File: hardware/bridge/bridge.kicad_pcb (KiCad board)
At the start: 2 copper layers, 45 x 80 mm, 72 parts, among them J1 XT30U-M, J10 PA5 breakout, J2 Seg A, J3 Seg B, J4 Seg C, J5 Seg D, J6 Head, J7 OLED, J8 Power button, J9 Ext 5V, Q1 NCE40P70K, Q2 2N7002, Q3 2N7002, Q4 MMBT3906, Q5 2N7002, U1 LMR51606XDBVR, U2 WeAct STM32G474 QFN48, U3 LSM6DSV16X breakout

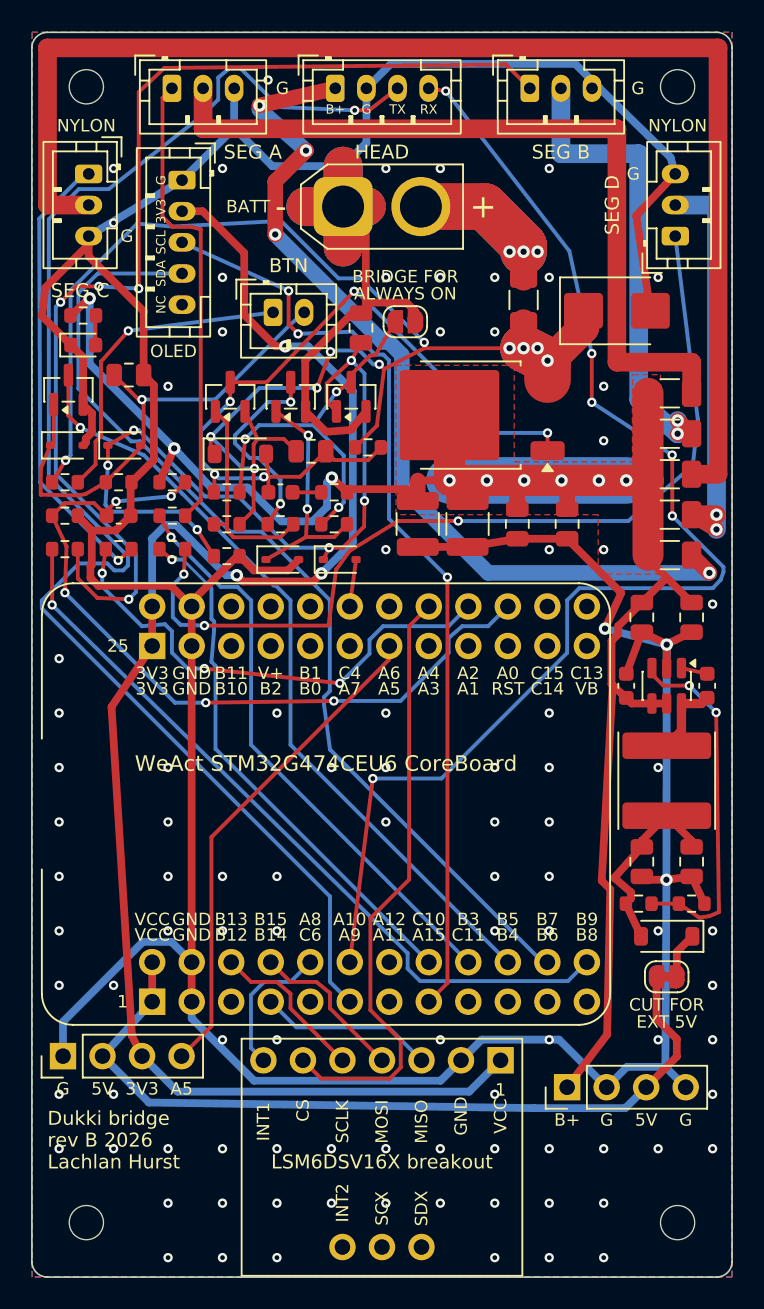
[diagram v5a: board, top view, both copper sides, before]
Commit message: Bridge PCB: second pre-order review fixes
- R14 220k to 100k (C25803, already on the board): a 70 ms tap latches
  at an 18 V pack with worst-case parts (220k needed about 150 ms).
- Buck feedback re-routed: from U1's FB pin straight to the bottom layer
  and down the west side to the divider, 17 mm, at least 1.9 mm from
  switch-node copper (it ran between the CB and SW pins and 0.22 mm
  beside L1's switch pad).
- Local copper: F3's segment B vias moved off its output pad; D2's
  ground pad solid with two stitching vias; 0.75 mm clearance round the
  XT30's + pad and a shorter ground bar beside it; JP2's ground pad on
  thermal spokes; a second via at two of VHEAD's layer changes.
- Silkscreen: J2's G above its own pin 3, clear of HEAD's B+; label
  strokes 0.15 mm; the IMU's VCC label clear of the pin-1 mark.
- Docs: the WeAct row rule in hardware/kicad/README.md, the head block
  diagram's UART direction, the carrier's exceptions in hardware.md 5.8,
  and corrected hold-up, tap and part-count figures in bridge-pcb.md.
- DRC clean with schematic parity; JLC package (30 BOM lines), PDFs and
  render regenerated.
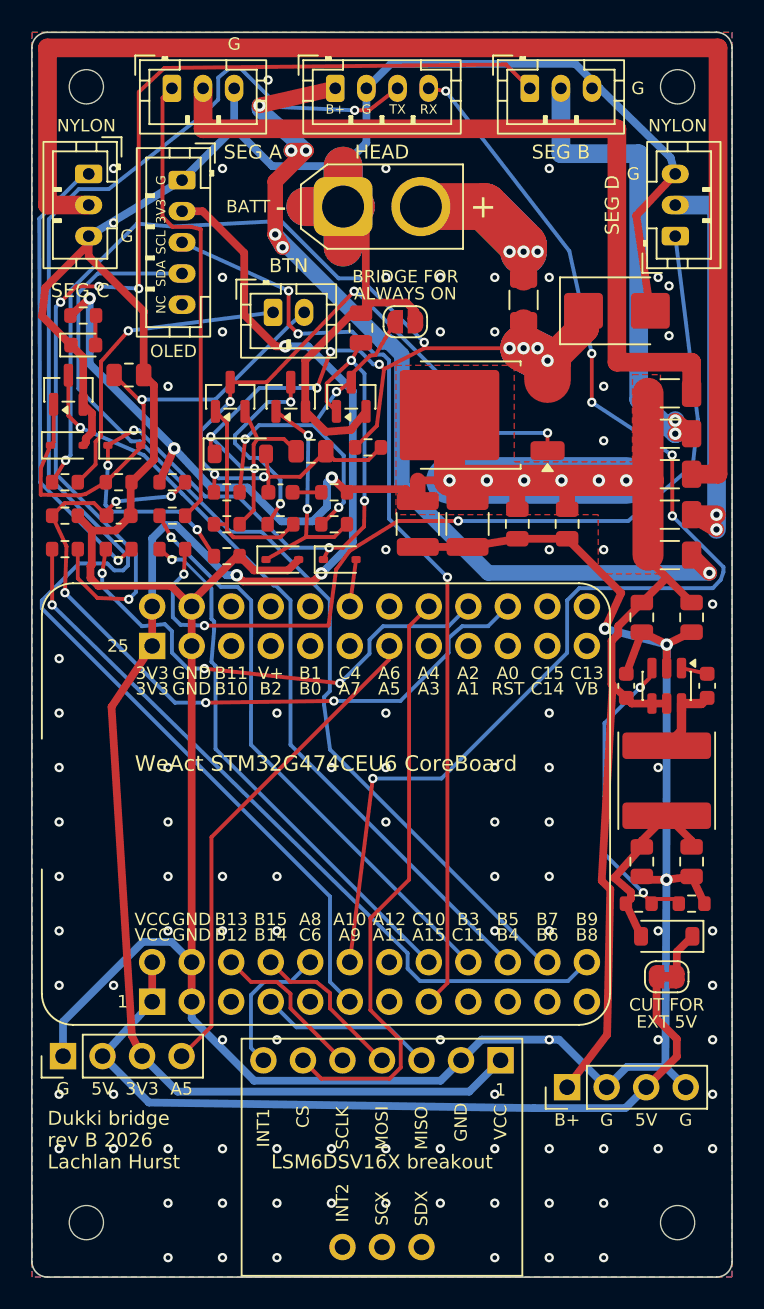
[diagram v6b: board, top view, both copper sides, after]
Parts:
- R14: value 220k -> 100k
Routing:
- net /BUCK_FB: track 23.0 -> 17.4 mm
- net /VHEAD: track 58.9 -> 62.7 mm, vias 4 -> 6
- net GND: track 303.2 -> 301.8 mm, vias 98 -> 99
